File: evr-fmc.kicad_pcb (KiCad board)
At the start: 6 copper layers, 84 x 69 mm, 234 parts, among them J1 MMCX, J10 MMCX, J11 MMCX, J12 MMCX, J13 MMCX, J14 MMCX, J15 MMCX, J16 MMCX, J17 MMCX, J18 MMCX, J19 WP Jumper, J2 MMCX, J20 MMCX, J21 MMCX, J3 MMCX, J4 MMCX, J5 MMCX, J6 MMCX, J7 MMCX, J8 MMCX, J9 MMCX, P1 ASP-134488-01, Q1 FDN335N, Q2 FDN335N, T1 TCM2-43X+, T2 TCM2-43X+, T3 TCM2-43X+, T4 TCM2-43X+, U1 SN74LVC3G34DCT, U10 SN74LVC3G34DCT, U11 SN74LVC3G34DCT, U12 SN74LVC3G34DCT, U13 SN74LVC3G34DCT, U14 SN74LVC3G34DCT, U15 SN74LVC3G34DCT, U16 SN74LVC3G34DCT, U17 SN74LVC3G34DCT, U18 SI5394, U19 SI5394, U2 SN74LVC3G34DCT, U20 TLV75733PDBV, U21 TLV75718PDBV, U22 TPS562200, U23 74AVC4T245, U25 74AVC4T245, U26 74LVC8T245, U27 74LVC8T245, U3 SN74LVC3G34DCT, U4 SN74LVC3G34DCT, U5 SN74LVC3G34DCT, U6 SN74LVC3G34DCT, U7 SN74LVC3G34DCT, U8 SN74LVC3G34DCT, U9 AT24C64D, Y1 CX3225SB48000D0FPJC1, Y2 CX3225SB48000D0FPJC1

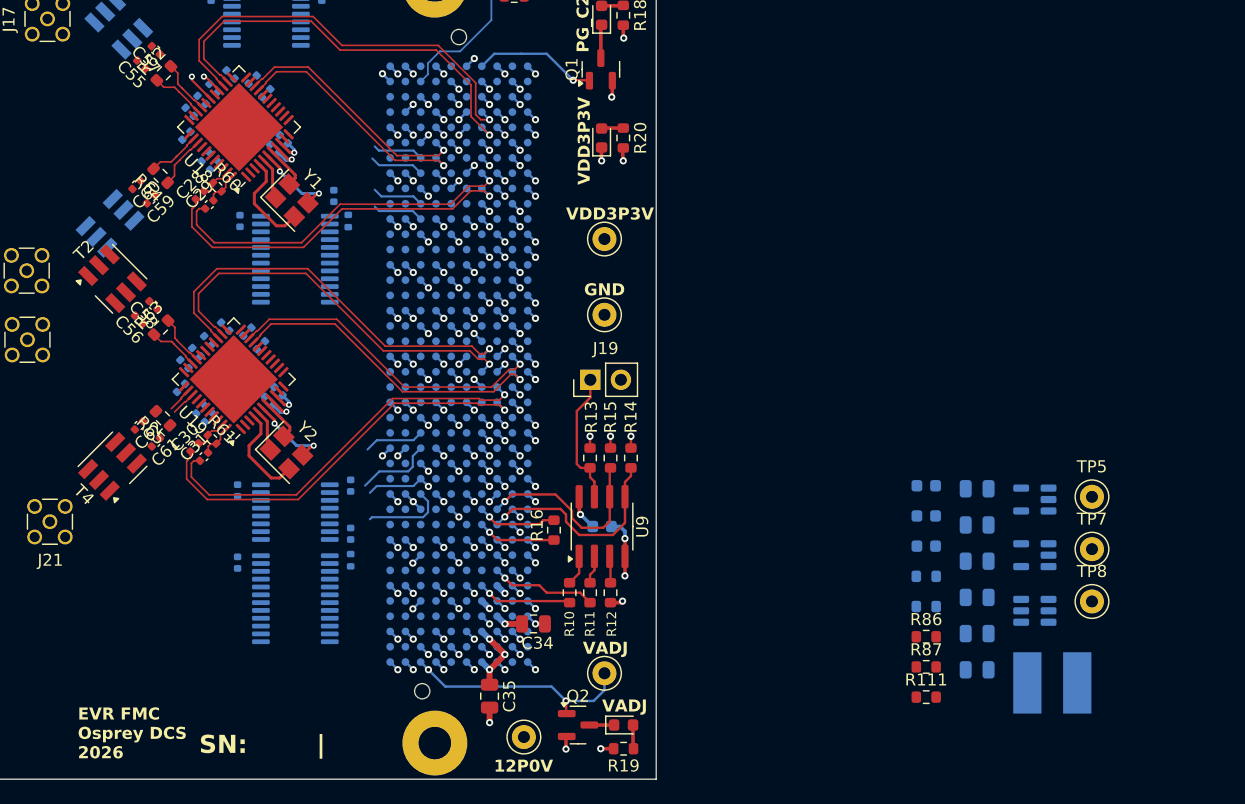
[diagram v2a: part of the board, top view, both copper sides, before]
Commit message: Schematic Updates
-Added Heartbeat LED
-Assigned Jitter cleaner OE to FPGA pins
-Changed LDO parts
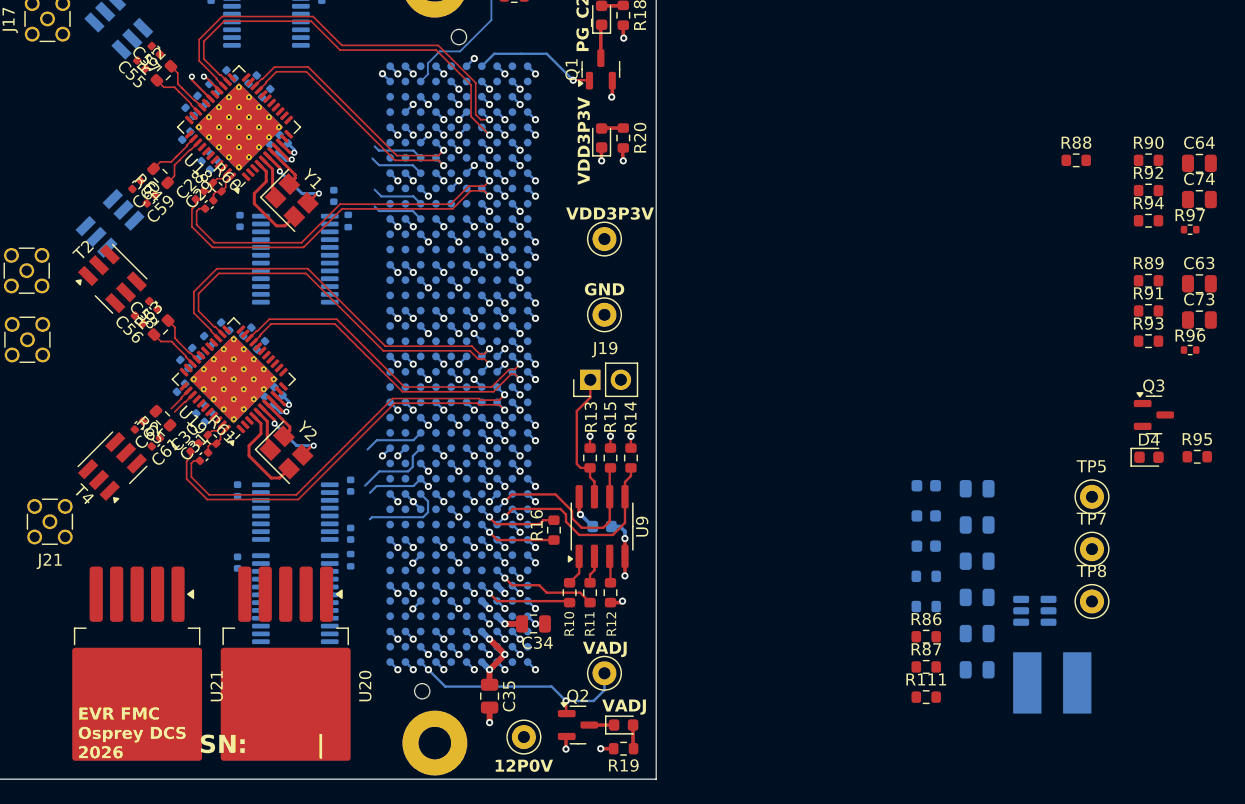
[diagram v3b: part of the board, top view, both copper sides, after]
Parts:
- added C63: 10uF, Capacitor_SMD:C_0805_2012Metric, F.Cu at (236.2, 98.8)
- added C64: 10uF, Capacitor_SMD:C_0805_2012Metric, F.Cu at (236.2, 88.8)
- added C73: 10uF, Capacitor_SMD:C_0805_2012Metric, F.Cu at (236.2, 101.8)
- added C74: 10uF, Capacitor_SMD:C_0805_2012Metric, F.Cu at (236.2, 91.8)
- added D4: LED_Green, LED_SMD:LED_0603_1608Metric, F.Cu at (232.0, 113.2)
- added Q3: FDN335N, Package_TO_SOT_SMD:SOT-23, F.Cu at (232.4, 109.7)
- added R88: 0R, Resistor_SMD:R_0603_1608Metric, F.Cu at (225.9, 88.6)
- added R89: 4.75k, Resistor_SMD:R_0603_1608Metric, F.Cu at (231.9, 98.6)
- added R90: 4.75k, Resistor_SMD:R_0603_1608Metric, F.Cu at (231.9, 88.6)
- added R91: 4.75k, Resistor_SMD:R_0603_1608Metric, F.Cu at (231.9, 101.1)
- added R92: 4.75k, Resistor_SMD:R_0603_1608Metric, F.Cu at (231.9, 91.1)
- added R93: 4.75k, Resistor_SMD:R_0603_1608Metric, F.Cu at (231.9, 103.6)
- added R94: 4.75k, Resistor_SMD:R_0603_1608Metric, F.Cu at (231.9, 93.6)
- added R95: 1k, Resistor_SMD:R_0603_1608Metric, F.Cu at (236.0, 113.2)
- added R96: 4.75k, Resistor_SMD:R_0402_1005Metric, F.Cu at (235.4, 104.3)
- added R97: 4.75k, Resistor_SMD:R_0402_1005Metric, F.Cu at (235.4, 94.3)
- U18, U19: footprint Package_DFN_QFN:QFN-44-1EP_7x7mm_P0.5mm_EP5.2x5.2mm -> rf-input-fmc:QFN-44-1EP_7x7mm_P0.5mm_EP5.2x5.2mm_ThermalVias
- U20: value TLV75733PDBV -> TPS75633; footprint Package_TO_SOT_SMD:SOT-23-5 -> Package_TO_SOT_SMD:TO-263-5_TabPin3; moved to F.Cu
- U21: value TLV75718PDBV -> TPS75618; footprint Package_TO_SOT_SMD:SOT-23-5 -> Package_TO_SOT_SMD:TO-263-5_TabPin3; moved to F.Cu
- moved U21 75.4 mm to (147.8, 132.3), turned to -90 degrees
- moved U20 64.2 mm to (160.2, 132.3), turned to -90 degrees
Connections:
- net /Jitter Cleaner0/SPI_OE renamed /Jitter Cleaner0/OE
- net /Jitter Cleaner1/SPI_OE renamed /Jitter Cleaner1/OE
- C46 pad 1: /Power/4P3V -> Net-(U20-EN)
- C47 pad 1: /Power/3P3V -> /Jitter Cleaner0/VDDA
- C48 pad 1: +12V_FMC -> Net-(U22-EN)
- C49 pad 1: +12V_FMC -> Net-(U22-EN)
- P1 pad C26: unconnected-(P1-PadC26) -> /FMC/Cleaner_~{OE}_0
- P1 pad C27: unconnected-(P1-PadC27) -> /FMC/Heartbeat_LED
- P1 pad H22: unconnected-(P1-PadH22) -> /FMC/Cleaner_~{OE}_1
- R111 pad 2: /Power/4P3V -> Net-(U20-EN)
- U20 pad 1: /Power/4P3V -> Net-(U20-EN)
- U20 pad 2: GND -> Net-(U20-EN)
- U20 pad 3: /Power/4P3V -> GND
- U20 pad 4: unconnected-(U20-NC-Pad4) -> Net-(U20-OUT)
- U20 pad 5: Net-(U20-OUT) -> unconnected-(U20-NC-Pad5)
- U21 pad 1: /Power/3P3V -> /Jitter Cleaner0/VDDA
- U21 pad 2: GND -> /Jitter Cleaner0/VDDA
- U21 pad 3: /Power/3P3V -> GND
- U21 pad 4: unconnected-(U21-NC-Pad4) -> Net-(U21-OUT)
- U21 pad 5: Net-(U21-OUT) -> unconnected-(U21-NC-Pad5)
- U22 pad 3: +12V_FMC -> Net-(U22-EN)
- U22 pad 5: +12V_FMC -> Net-(U22-EN)
- U23 pad 14: GND -> /Jitter Cleaner0/OE_Faults
- U23 pad 15: GND -> /Jitter Cleaner0/OE_Faults
- U25 pad 14: GND -> /Jitter Cleaner1/OE_Faults
- U25 pad 15: GND -> /Jitter Cleaner1/OE_Faults

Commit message: Finalized Schematic and Updated Layout
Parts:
- removed L2, L3, L4, L5: 60R@100Mhz; 3.5A, Inductor_SMD:L_0805_2012Metric
- added C75: 1uF, Capacitor_SMD:C_0603_1608Metric, F.Cu at (154.0, 105.4)
- added C76: 10uF, Capacitor_SMD:C_0805_2012Metric, F.Cu at (154.5, 99.1)
- added C77: 1uF, Capacitor_SMD:C_0603_1608Metric, F.Cu at (158.0, 97.1)
- added C78: 10uF, Capacitor_SMD:C_0805_2012Metric, F.Cu at (158.2, 103.5)
- added R98: 0R, Resistor_SMD:R_0603_1608Metric, F.Cu at (154.5, 97.1)
- added R99: 0R, Resistor_SMD:R_0603_1608Metric, F.Cu at (158.2, 105.3)
- added TP6: 3P3V, TestPoint:TestPoint_Keystone_5000-5004_Miniature, F.Cu at (150.0, 116.4)
- added TP9: 1P8V, TestPoint:TestPoint_Keystone_5000-5004_Miniature, F.Cu at (140.8, 111.8)
- added U24: TLV75733PDBV, Package_TO_SOT_SMD:SOT-23-5, F.Cu at (154.4, 102.4)
- added U28: TLV75718PDBV, Package_TO_SOT_SMD:SOT-23-5, F.Cu at (158.2, 100.1)
- C1, C11, C13, C15, C3, C5, C7, C73, C9, R69, R71, R72, R73, R74, R75, R76, R77, R78, R79, R80, R81, R82, R83, R84, R85, R96, R97: moved to B.Cu
- C46, C47, C48, C49, C50, C51, C52, C53, C54, L1, R66, R67, T1, T3, U1, U11, U13, U15, U17, U22, U4, U6, U8: moved to F.Cu
- R1, R2, R23, R24, R25, R29, R30, R31, R35, R36, R37, R38, R42, R43, R44, R48, R49, R50, R54, R55, R56, R6, R7, R8: footprint Resistor_SMD:R_0805_2012Metric -> Resistor_SMD:R_0603_1608Metric
- R21, R22, R26, R27, R28, R3, R32, R33, R34, R39, R4, R40, R41, R45, R46, R47, R5, R51, R52, R53, R57, R58, R59, R9: footprint Resistor_SMD:R_0805_2012Metric -> Resistor_SMD:R_0603_1608Metric; moved to F.Cu
- R89, R90, R91, R92, R93, R94: footprint Resistor_SMD:R_0603_1608Metric -> Resistor_SMD:R_0402_1005Metric; moved to B.Cu
- U20: value TPS75633 -> TLV75733PDBV; footprint Package_TO_SOT_SMD:TO-263-5_TabPin3 -> Package_TO_SOT_SMD:SOT-23-5
- U21: value TPS75618 -> TLV75718PDBV; footprint Package_TO_SOT_SMD:TO-263-5_TabPin3 -> Package_TO_SOT_SMD:SOT-23-5
- moved R85 95.1 mm to (137.0, 131.7), turned to 90 degrees
- moved TP7 93.2 mm to (143.4, 80.2)
- moved C74 89.0 mm to (147.4, 98.6)
- moved R77 89.0 mm to (136.9, 103.6), turned to 90 degrees
- moved C73 88.0 mm to (150.0, 83.8), turned to -135 degrees
- moved R75 84.0 mm to (136.9, 96.2), turned to 90 degrees
- moved TP8 83.4 mm to (144.1, 131.9)
- moved R96 83.0 mm to (158.4, 73.2)
- moved R81 79.9 mm to (136.9, 118.2), turned to 90 degrees
- moved C64 79.9 mm to (162.3, 119.4), turned to 45 degrees
- moved TP5 79.4 mm to (150.6, 95.8)
- moved R88 77.4 mm to (165.6, 137.0), turned to 180 degrees
- moved R84 77.2 mm to (121.7, 125.8), turned to 90 degrees
- moved R79 77.1 mm to (136.9, 110.9), turned to 90 degrees
- moved R97 76.4 mm to (161.2, 112.8), turned to 180 degrees
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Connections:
- net Net-(C37-Pad1) renamed /Jitter Cleaner1/VDDA
- net Net-(C41-Pad1) renamed /Jitter Cleaner1/VDD
- C17 pad 1: Net-(C17-Pad1) -> /Jitter Cleaner0/VDDA
- C18 pad 1: Net-(C17-Pad1) -> /Jitter Cleaner0/VDDA
- C23 pad 1: Net-(C23-Pad1) -> /Jitter Cleaner0/VDD
- C24 pad 1: Net-(C23-Pad1) -> /Jitter Cleaner0/VDD
- C25 pad 1: Net-(C23-Pad1) -> /Jitter Cleaner0/VDD
- C26 pad 1: Net-(C23-Pad1) -> /Jitter Cleaner0/VDD
- C63 pad 1: Net-(C17-Pad1) -> /Jitter Cleaner0/VDDA
- C73 pad 1: Net-(C23-Pad1) -> /Jitter Cleaner0/VDD
- U18 pad 21: Net-(C23-Pad1) -> /Jitter Cleaner0/VDD
- U18 pad 32: Net-(C23-Pad1) -> /Jitter Cleaner0/VDD
- U18 pad 39: Net-(C23-Pad1) -> /Jitter Cleaner0/VDD
- U18 pad 40: Net-(C23-Pad1) -> /Jitter Cleaner0/VDD
- U18 pad 8: Net-(C17-Pad1) -> /Jitter Cleaner0/VDDA
- U18 pad 9: Net-(C17-Pad1) -> /Jitter Cleaner0/VDDA
- U20 pad 2: Net-(U20-EN) -> GND
- U20 pad 3: GND -> Net-(U20-EN)
- U20 pad 4: Net-(U20-OUT) -> unconnected-(U20-NC-Pad4)
- U20 pad 5: unconnected-(U20-NC-Pad5) -> Net-(U20-OUT)
- U21 pad 2: /Jitter Cleaner0/VDDA -> GND
- U21 pad 3: GND -> /Jitter Cleaner0/VDDA
- U21 pad 4: Net-(U21-OUT) -> unconnected-(U21-NC-Pad4)
- U21 pad 5: unconnected-(U21-NC-Pad5) -> Net-(U21-OUT)
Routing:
- net GND: track 156.4 -> 202.6 mm, vias 166 -> 167
- net VDD3P3V: track 13.5 -> 59.5 mm, vias 8 -> 24
- net /FMC/Recovered_CLK_1.N: track 33.1 -> 45.1 mm
- net /FMC/Recovered_CLK_1.P: track 34.0 -> 46.1 mm
- net /Digital IO/D_Output0: track 0.00 -> 9.38 mm, vias 0 -> 1
- net Net-(U17-3Y): track 0.00 -> 6.25 mm
- net Net-(U8-3Y): track 0.00 -> 6.25 mm
- net Net-(U6-3Y): track 0.00 -> 6.25 mm
- net Net-(U13-3Y): track 0.00 -> 6.25 mm
- net Net-(U1-3Y): track 0.00 -> 6.25 mm
- net Net-(U7-3Y): track 0.00 -> 6.25 mm
- net Net-(U5-3Y): track 0.00 -> 6.25 mm
- net Net-(U3-3Y): track 0.00 -> 6.25 mm
- net Net-(U16-3Y): track 0.00 -> 6.25 mm
- net Net-(U14-3Y): track 0.00 -> 6.25 mm
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
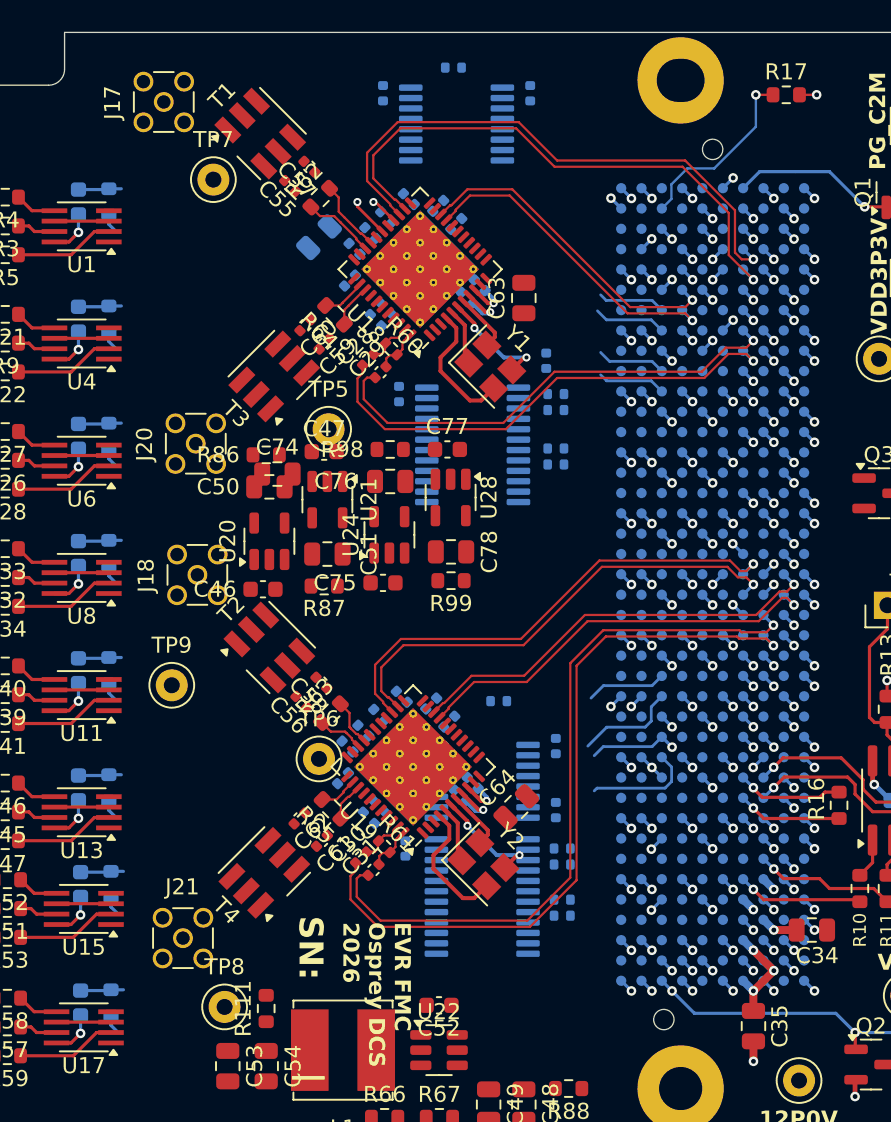
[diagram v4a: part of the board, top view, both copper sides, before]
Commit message: Updated Layout
- parts floor planed
- need to finish digital IO routing
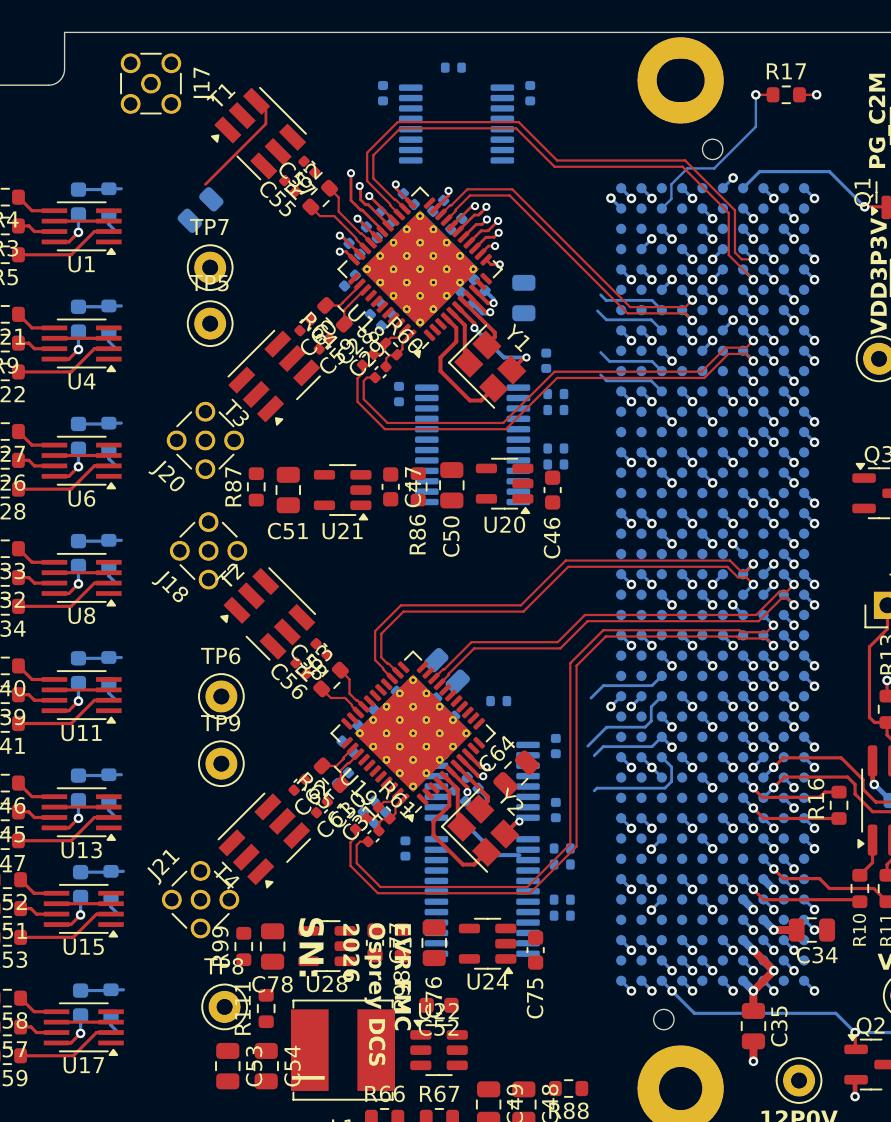
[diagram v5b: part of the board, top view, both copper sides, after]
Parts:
- C63, C74: moved to B.Cu
- moved C77 31.2 mm to (153.5, 127.9), turned to -90 degrees
- moved R98 30.8 mm to (155.2, 127.9), turned to 90 degrees
- moved U28 29.1 mm to (150.5, 128.1), turned to 180 degrees
- moved C76 29.0 mm to (157.2, 127.9), turned to 90 degrees
- moved C78 27.1 mm to (147.1, 128.1), turned to 90 degrees
- moved U24 26.3 mm to (160.5, 128.0), turned to 180 degrees
- moved R99 26.3 mm to (145.3, 128.1), turned to 90 degrees
- moved C75 24.9 mm to (163.5, 128.4), turned to 90 degrees
- moved C46 19.1 mm to (164.6, 99.6), turned to 90 degrees
- moved C74 16.2 mm to (158.0, 110.9), turned to -45 degrees
- moved U20 15.1 mm to (161.6, 99.2), turned to 180 degrees
- moved C50 11.4 mm to (158.3, 99.3), turned to 90 degrees
- moved TP5 9.92 mm to (143.2, 89.2)
- moved R86 9.71 mm to (156.2, 99.4), turned to 90 degrees
- moved C73 7.59 mm to (142.6, 82.1)
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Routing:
- net Net-(J17-In): track 0.00 -> 7.01 mm
- net P1_VADJ: track 20.4 -> 26.3 mm, vias 3 -> 6
- net Net-(U19-XB): track 7.00 -> 2.99 mm
- net /FMC/Cleaner_SPI_1.OE: track 0.00 -> 4.01 mm
- net /Jitter Cleaner0/VDD: track 0.00 -> 3.98 mm, vias 0 -> 2
- net /Jitter Cleaner0/LOL: track 0.00 -> 3.32 mm, vias 0 -> 1
- net /Jitter Cleaner0/RST: track 0.00 -> 2.47 mm, vias 0 -> 1
- net /Jitter Cleaner0/SPI_SDO: track 0.00 -> 2.37 mm, vias 0 -> 1
- net /FMC/Recovered_CLK_1.P: track 46.1 -> 44.0 mm
- net /FMC/Recovered_CLK_1.N: track 45.1 -> 43.0 mm
- net /Jitter Cleaner0/LOS_XO: track 2.49 -> 4.51 mm
- net /Jitter Cleaner0/SPI_CS: track 0.00 -> 1.92 mm, vias 0 -> 1
- net /Jitter Cleaner0/SPI_CLK: track 0.00 -> 1.90 mm, vias 0 -> 1
- net /Jitter Cleaner0/SPI_SDI: track 0.00 -> 1.12 mm, vias 0 -> 1
- net /Jitter Cleaner0/INTR: track 0.00 -> 1.10 mm, vias 0 -> 1
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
